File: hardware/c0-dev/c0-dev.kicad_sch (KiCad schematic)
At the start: 17 parts, among them J1 2913730000, J10 2913730000, J11 2913730000, J12 2913710000, J13 2913730000, J14 2913730000, J2 2913710000, J3 2913730000, J4 2913730000, J5 2913710000, J6 2913730000, J7 2913730000, J8 2913710000, J9 2913730000

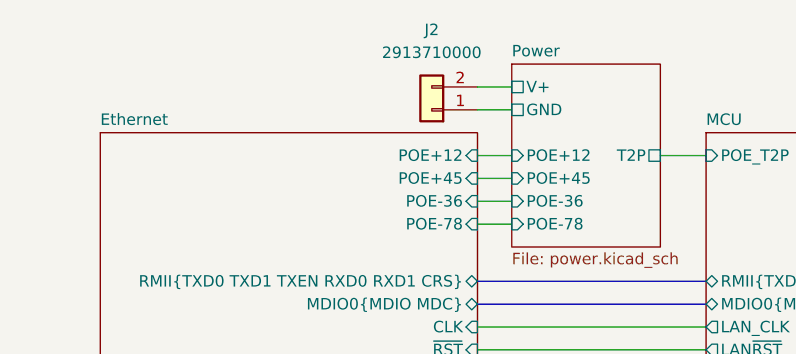
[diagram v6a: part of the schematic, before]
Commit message: added 2-pin terminals
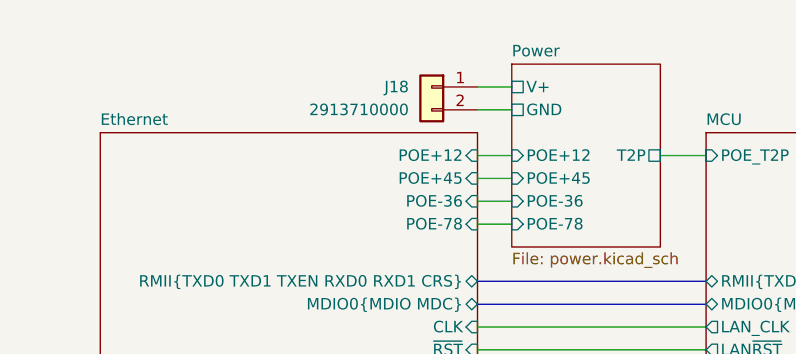
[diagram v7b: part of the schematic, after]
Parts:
- removed J2: 2913710000, symbol Connector_Generic:Conn_01x02
- added J18: 2913710000, conduit:2913710000, symbol Connector_Generic:Conn_01x02
- J12, J5, J8: footprint (none) -> conduit:2913710000
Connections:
- net Power/GND: now also J18.2 (Pin_2)
- net Power/V+: now also J18.1 (Pin_1)
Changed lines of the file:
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@@
+	(symbol
+		(lib_id "Connector_Generic:Conn_01x02")
+		(at 69.85 22.86 0)
+		(mirror y)
+		(unit 1)
+		(body_style 1)
+		(exclude_from_sim no)
+		(in_bom yes)
+		(on_board yes)
+		(in_pos_files yes)
+		(dnp no)
+		(property "Reference" "J18"
+			(at 67.31 22.8599 0)
+			(show_name no)
+			(do_not_autoplace no)
+			(effects
+				(font
+					(size 1.27 1.27)
+				)
+				(justify left)
+			)
+		)
+		(property "Value" "2913710000"
+			(at 67.31 25.3999 0)
+			(show_name no)
+			(do_not_autoplace no)
+			(effects
+				(font
+					(size 1.27 1.27)
+				)
+				(justify left)
+			)
+		)
+		(property "Footprint" "conduit:2913710000"
+			(at 69.85 22.86 0)
+			(hide yes)
+			(show_name no)
+			(do_not_autoplace no)
+			(effects
+				(font
+					(size 1.27 1.27)
+				)
+			)
+		)
+		(property "Datasheet" "https://datasheet.weidmueller.com/pdf/en/2913710000/scope/2/"
+			(at 69.85 22.86 0)
+			(hide yes)
+			(show_name no)
+			(do_not_autoplace no)
+			(effects
+				(font
+					(size 1.27 1.27)
+				)
+			)
+		)
+		(property "Description" "Generic connector, single row, 01x02, script generated (kicad-library-utils/schlib/autogen/connector/)"
+			(at 69.85 22.86 0)
+			(hide yes)
+			(show_name no)
+			(do_not_autoplace no)
+			(effects
+				(font
+					(size 1.27 1.27)
+				)
+			)
+		)
+		(pin "2"
+		)
+		(pin "1"
+		)
+		(instances
+			(project "c0-dev"
+				(path "/b8347a0e-ad04-4414-969d-3c64a611d74e"
+					(reference "J18")
+					(unit 1)
+				)
+			)
+		)
+	)
+	(symbol
+		(lib_id "Connector_Generic:Conn_01x02")
+		(at 217.17 86.36 0)
+		(unit 1)
+		(body_style 1)
+		(exclude_from_sim no)
+		(in_bom yes)
+		(on_board yes)
+		(in_pos_files yes)
+		(dnp no)
+		(fields_autoplaced yes)
+		(property "Reference" "J8"
+			(at 219.71 86.3599 0)
+			(show_name no)
+			(do_not_autoplace no)
+			(effects
+				(font
+					(size 1.27 1.27)
+				)
+				(justify left)
+			)
+		)
+		(property "Value" "2913710000"
+			(at 219.71 88.8999 0)
+			(show_name no)
+			(do_not_autoplace no)
+			(effects
+				(font
+					(size 1.27 1.27)
+				)
+				(justify left)
+			)
+		)
+		(property "Footprint" "conduit:2913710000"
+			(at 217.17 86.36 0)
+			(hide yes)
+			(show_name no)
+			(do_not_autoplace no)
+			(effects
+				(font
+					(size 1.27 1.27)
+				)
+			)
+		)
+		(property "Datasheet" "https://datasheet.weidmueller.com/pdf/en/2913710000/scope/2/"
+			(at 217.17 86.36 0)
+			(hide yes)
+			(show_name no)
+			(do_not_autoplace no)
+			(effects
+				(font
+					(size 1.27 1.27)
+				)
+			)
+		)
+		(property "Description" "Generic connector, single row, 01x02, script generated (kicad-library-utils/schlib/autogen/connector/)"
+			(at 217.17 86.36 0)
+			(hide yes)
+			(show_name no)
+			(do_not_autoplace no)
+			(effects
+				(font
+					(size 1.27 1.27)
+				)
+			)
+		)
+		(pin "2"
+		)
+		(pin "1"
+		)
+		(instances
+			(project "c0-dev"
+				(path "/b8347a0e-ad04-4414-969d-3c64a611d74e"
+					(reference "J8")
+					(unit 1)
+				)
+			)
+		)
+	)
 	(symbol
 		(lib_id "Connector_Generic:Conn_01x02")
@@
 			)
 		)
-		(property "Footprint" ""
+		(property "Footprint" "conduit:2913710000"
 			(at 217.17 129.54 0)
 			(hide yes)
@@
 				(path "/b8347a0e-ad04-4414-969d-3c64a611d74e"
 					(reference "J12")
-					(unit 1)
-				)
-			)
-		)
-	)
-	(symbol
-		(lib_id "Connector_Generic:Conn_01x02")
-		(at 69.85 25.4 180)
-		(unit 1)
-		(body_style 1)
-		(exclude_from_sim no)
-		(in_bom yes)
-		(on_board yes)
-		(in_pos_files yes)
-		(dnp no)
-		(fields_autoplaced yes)
-		(property "Reference" "J2"
-			(at 69.85 16.51 0)
-			(show_name no)
-			(do_not_autoplace no)
-			(effects
-				(font
-					(size 1.27 1.27)
-				)
-			)
-		)
-		(property "Value" "2913710000"
-			(at 69.85 19.05 0)
-			(show_name no)
-			(do_not_autoplace no)
-			(effects
-				(font
-					(size 1.27 1.27)
-				)
-			)
-		)
-		(property "Footprint" ""
-			(at 69.85 25.4 0)
-			(hide yes)
-			(show_name no)
-			(do_not_autoplace no)
-			(effects
-				(font
-					(size 1.27 1.27)
-				)
-			)
-		)
-		(property "Datasheet" "https://datasheet.weidmueller.com/pdf/en/2913710000/scope/2/"
-			(at 69.85 25.4 0)
-			(hide yes)
-			(show_name no)
-			(do_not_autoplace no)
-			(effects
-				(font
-					(size 1.27 1.27)
-				)
-			)
-		)
-		(property "Description" "Generic connector, single row, 01x02, script generated (kicad-library-utils/schlib/autogen/connector/)"
-			(at 69.85 25.4 0)
-			(hide yes)
-			(show_name no)
-			(do_not_autoplace no)
-			(effects
-				(font
-					(size 1.27 1.27)
-				)
-			)
-		)
-		(pin "2"
-		)
-		(pin "1"
-		)
-		(instances
-			(project "c0-dev"
-				(path "/b8347a0e-ad04-4414-969d-3c64a611d74e"
-					(reference "J2")
 					(unit 1)
 				)
@@
 			)
 		)
-		(property "Footprint" ""
+		(property "Footprint" "conduit:2913710000"
 			(at 217.17 48.26 0)
 			(hide yes)
@@
 					(unit 1)
 				)
-			)
-		)
-	)
-	(symbol
-		(lib_id "Connector_Generic:Conn_01x02")
-		(at 217.17 86.36 0)
-		(unit 1)
-		(body_style 1)
-		(exclude_from_sim no)
-		(in_bom yes)
-		(on_board yes)
-		(in_pos_files yes)
-		(dnp no)
-		(fields_autoplaced yes)
-		(property "Reference" "J8"
-			(at 219.71 86.3599 0)
-			(show_name no)
-			(do_not_autoplace no)
-			(effects
-				(font
-					(size 1.27 1.27)
-				)
-				(justify left)
-			)
-		)
-		(property "Value" "2913710000"
-			(at 219.71 88.8999 0)
-			(show_name no)
-			(do_not_autoplace no)
-			(effects
-				(font
-					(size 1.27 1.27)
-				)
-				(justify left)
-			)
-		)
-		(property "Footprint" ""
-			(at 217.17 86.36 0)
-			(hide yes)
-			(show_name no)
-			(do_not_autoplace no)
-			(effects
-				(font
-					(size 1.27 1.27)
-				)
-			)
-		)
-		(property "Datasheet" "https://datasheet.weidmueller.com/pdf/en/2913710000/scope/2/"
-			(at 217.17 86.36 0)
-			(hide yes)
-			(show_name no)
-			(do_not_autoplace no)
-			(effects
-				(font
-					(size 1.27 1.27)
-				)
-			)
-		)
-		(property "Description" "Generic connector, single row, 01x02, script generated (kicad-library-utils/schlib/autogen/connector/)"
-			(at 217.17 86.36 0)
-			(hide yes)
-			(show_name no)
-			(do_not_autoplace no)
-			(effects
-				(font
-					(size 1.27 1.27)
-				)
-			)
-		)
-		(pin "2"
-		)
-		(pin "1"
-		)
-		(instances
-			(project "c0-dev"
-				(path "/b8347a0e-ad04-4414-969d-3c64a611d74e"
-					(reference "J8")
-					(unit 1)
-				)

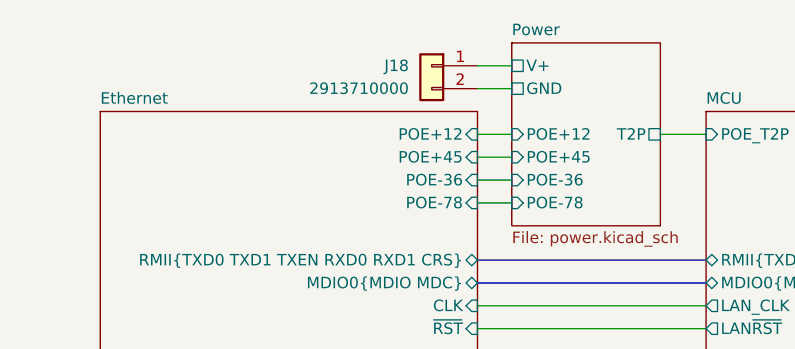
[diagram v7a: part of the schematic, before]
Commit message: annotation + new digital out
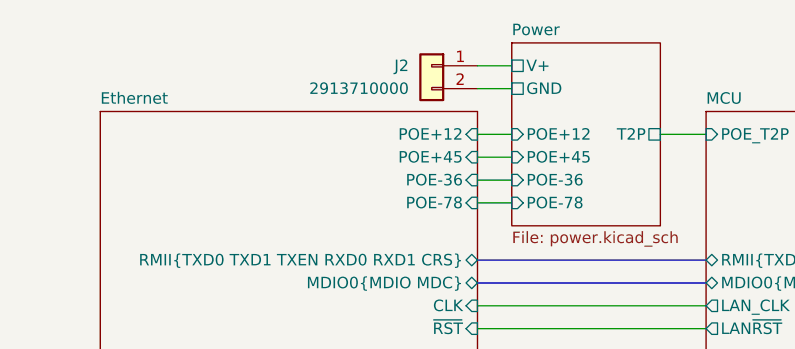
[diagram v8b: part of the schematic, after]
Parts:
- renumbered J18 to J2
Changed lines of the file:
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@@
 		(in_pos_files yes)
 		(dnp no)
-		(property "Reference" "J18"
+		(property "Reference" "J2"
 			(at 67.31 22.8599 0)
 			(show_name no)
@@
 			(project "c0-dev"
 				(path "/b8347a0e-ad04-4414-969d-3c64a611d74e"
-					(reference "J18")
+					(reference "J2")
 					(unit 1)
 				)
